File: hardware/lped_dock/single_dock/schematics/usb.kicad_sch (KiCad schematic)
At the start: 5 parts, among them J7 USB-C connector, U1 TPD4E02B04DQA

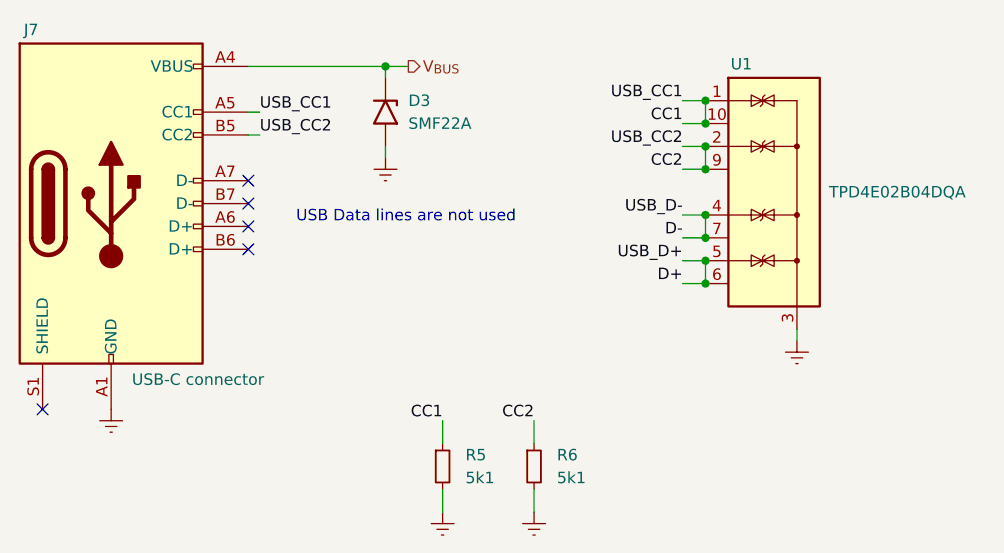
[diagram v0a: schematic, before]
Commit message: feat(hardware): add battery charger and connector to single charger
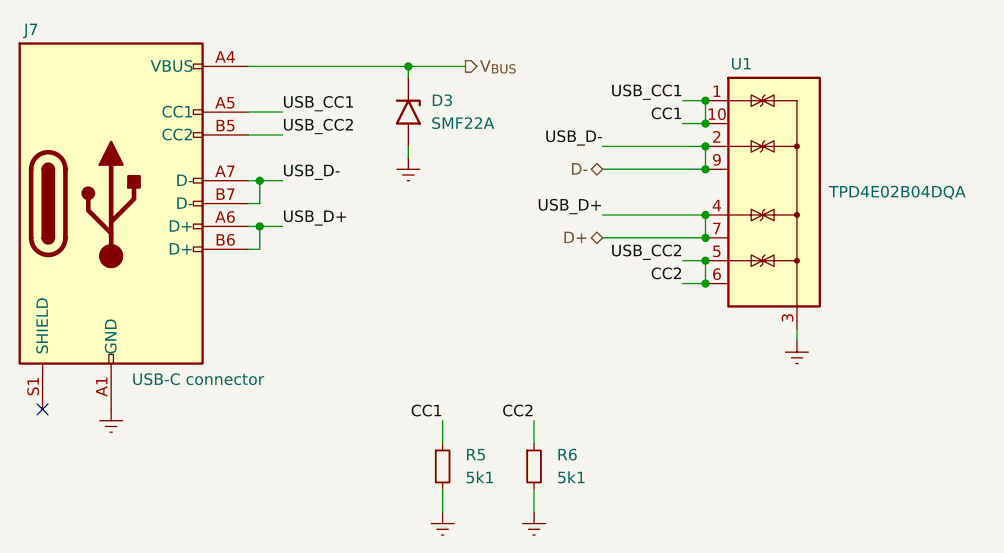
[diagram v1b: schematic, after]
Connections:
- net CC2: now also U1.5 (IO4), U1.6 (NC); no longer U1.2 (IO2), U1.9 (NC)
- net D+: now also J7.A6 (D+), J7.B6 (D+), U1.4 (IO3), U1.7 (NC); no longer U1.5 (IO4), U1.6 (NC)
- net D-: now also J7.A7 (D-), J7.B7 (D-), U1.2 (IO2), U1.9 (NC); no longer U1.4 (IO3), U1.7 (NC)
- no-connect marks 5 -> 1
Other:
- note removed: "USB Data lines are not used"
- moved on the sheet: D3
